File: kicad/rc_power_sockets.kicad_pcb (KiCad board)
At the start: 2 copper layers, 50 x 50 mm, 25 parts, among them IC1 ATTINY85, J1 PIR, J2 433MHZ, J3 433MHZ, P1 ICSP, P2 POWER_IN, Q1 NMOS, Q2 PMOS, U1 MCP1700T

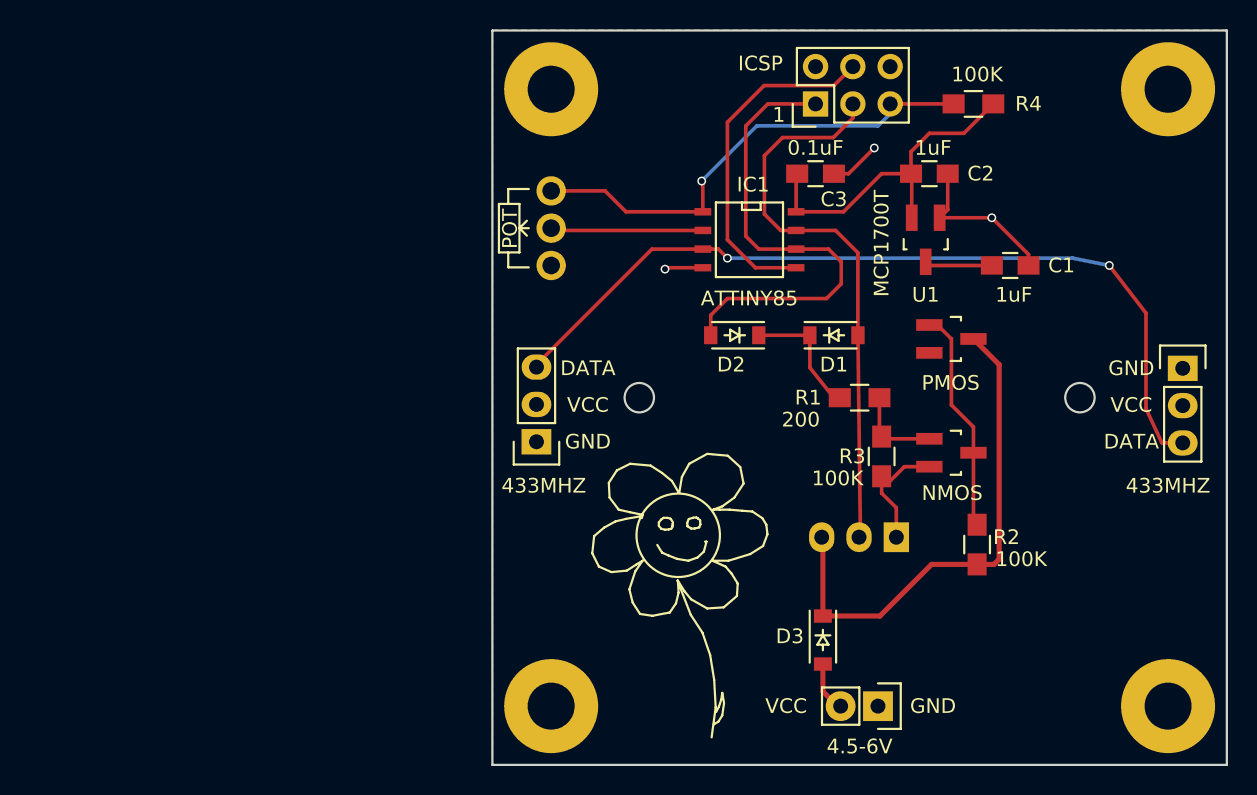
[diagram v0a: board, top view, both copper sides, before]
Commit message: Changed voltage regulator to handle higher input
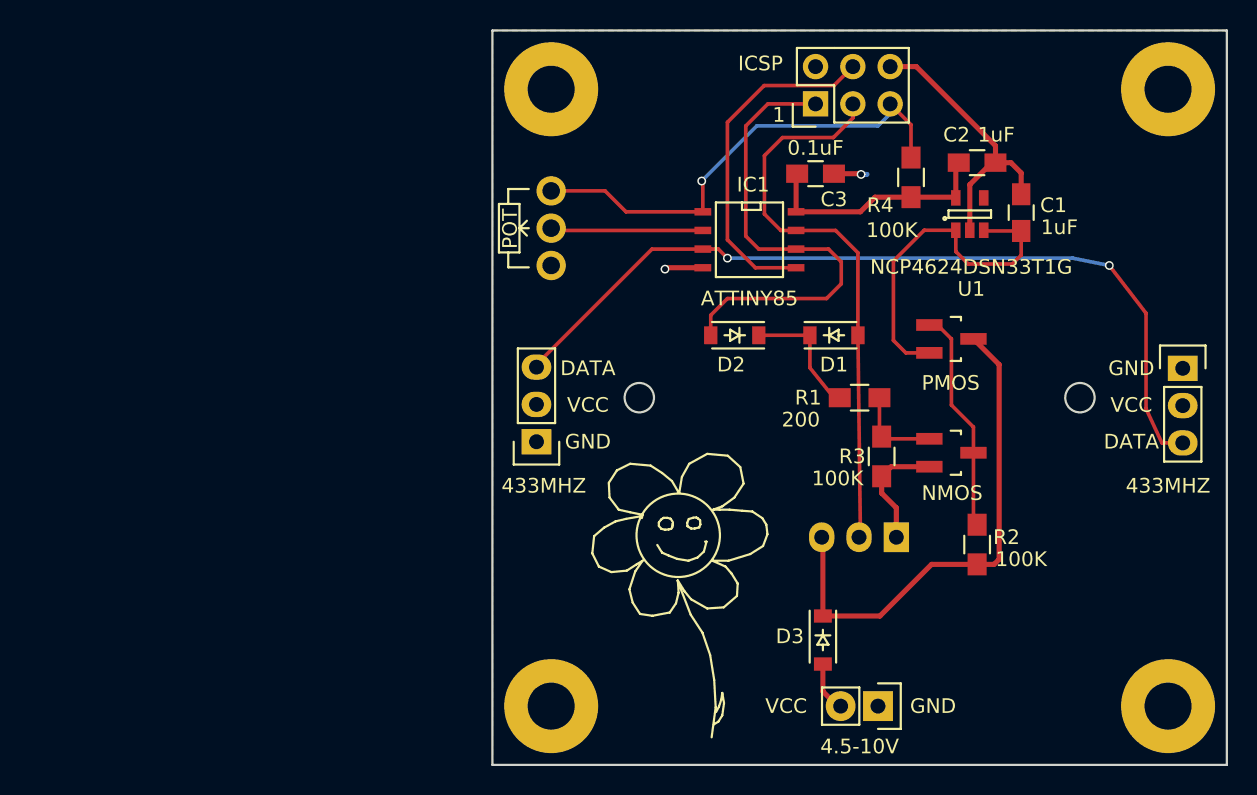
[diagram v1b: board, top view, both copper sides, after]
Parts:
- U1: value MCP1700T -> NCP4624DSN33T1G; footprint TO_SOT_Packages_SMD:SOT-23_Handsoldering -> SOT-23-5
- moved R4 6.56 mm to (148.5, 70.0), turned to 270 degrees
- moved C1 3.68 mm to (156.0, 72.4), turned to 90 degrees
- moved U1 3.47 mm to (152.5, 72.5), turned to 90 degrees
- moved C2 3.34 mm to (153.0, 69.0)
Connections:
- U1 pad 1: GND -> /SWITCH_POWER
- U1 pad 2: /3.3v -> GND
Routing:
- net /SWITCH_POWER: track 4.60 -> 24.0 mm
- net GND: track 25.4 -> 33.1 mm, vias 3 -> 2
- net /3.3v: track 23.0 -> 16.4 mm
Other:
- net class GND added: clearance 0.3, trace_width 0.35, via_dia 0.6, via_drill 0.4
- board text added: "4.5-10V"
- board text removed: "4.5-6V"

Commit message: Silkscreen update
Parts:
- U1: value NCP4624DSN33T1G -> 3.3V REG
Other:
- board text added: "March 2016"
- board text added: "https://github.com/theapi/rc_power_sockets"
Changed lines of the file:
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@@
-(kicad_pcb (version 4) (host pcbnew 4.0.1-stable)
+(kicad_pcb (version 4) (host pcbnew 4.0.2-4+6225~38~ubuntu14.04.1-stable)
   (general
     (links 48)
     (no_connects 0)
-    (area 119.924999 59.924999 170.075001 110.075001)
+    (area 118.275 58.575 171.208334 111.275)
     (thickness 1.6)
-    (drawings 21)
+    (drawings 23)
     (tracks 130)
     (zones 0)
@@
   (layers
     (0 F.Cu signal)
-    (31 B.Cu signal hide)
+    (31 B.Cu signal)
     (32 B.Adhes user)
     (33 F.Adhes user)
@@
     (tags "capacitor 0805")
     (attr smd)
-    (fp_text reference C2 (at -1.4 -1.9 180) (layer F.SilkS)
-      (effects (font (size 1 1) (thickness 0.15)))
-    )
-    (fp_text value 1uF (at 1.3 -1.9) (layer F.SilkS)
+    (fp_text reference C2 (at 1.75 -1.75 180) (layer F.SilkS)
+      (effects (font (size 1 1) (thickness 0.15)))
+    )
+    (fp_text value 1uF (at -1.25 -1.75) (layer F.SilkS)
       (effects (font (size 1 1) (thickness 0.15)))
     )
@@
     (tags "capacitor 0805")
     (attr smd)
-    (fp_text reference C3 (at 1.25 1.75) (layer F.SilkS)
-      (effects (font (size 1 1) (thickness 0.15)))
-    )
-    (fp_text value 0.1uF (at 0 -1.75) (layer F.SilkS)
+    (fp_text reference C3 (at 2.5 -1.75) (layer F.SilkS)
+      (effects (font (size 1 1) (thickness 0.15)))
+    )
+    (fp_text value 0.1uF (at -1 -1.75) (layer F.SilkS)
       (effects (font (size 1 1) (thickness 0.15)))
     )
@@
     (tags SOT-23-5)
     (attr smd)
-    (fp_text reference U1 (at -5.1 0.1 180) (layer F.SilkS)
-      (effects (font (size 1 1) (thickness 0.15)))
-    )
-    (fp_text value NCP4624DSN33T1G (at -3.6 0.1 180) (layer F.SilkS)
+    (fp_text reference U1 (at -3 0 180) (layer F.SilkS)
+      (effects (font (size 1 1) (thickness 0.15)))
+    )
+    (fp_text value "3.3V REG" (at -4.5 0 180) (layer F.SilkS)
       (effects (font (size 1 1) (thickness 0.15)))
     )
@@
     )
   )
+  (gr_text www.theapi.co.uk (at 144.75 85) (layer B.SilkS)
+    (effects (font (size 1 1) (thickness 0.15)) (justify mirror))
+  )
+  (gr_text https://github.com/theapi/rc_power_sockets (at 145.5 78.5) (layer B.SilkS)
+    (effects (font (size 1 1) (thickness 0.15)) (justify mirror))
+  )
   (gr_text 1 (at 139.5 65.75) (layer F.SilkS)
     (effects (font (size 1 1) (thickness 0.15)))
@@
     (effects (font (size 1 1) (thickness 0.15)))
   )
-  (gr_text www.theapi.co.uk (at 144.8 82.6) (layer B.SilkS)
-    (effects (font (size 1 1) (thickness 0.15)) (justify mirror))
-  )
-  (gr_text "RC Power Sockets v1.0" (at 145 80.6) (layer B.SilkS)
+  (gr_text "March 2016" (at 135.75 81) (layer B.SilkS)
     (effects (font (size 1 1) (thickness 0.15) italic) (justify mirror))
   )
+  (gr_text "RC Power Sockets v1.0" (at 150 81) (layer B.SilkS)
+    (effects (font (size 1 1) (thickness 0.15) italic) (justify mirror))
+  )

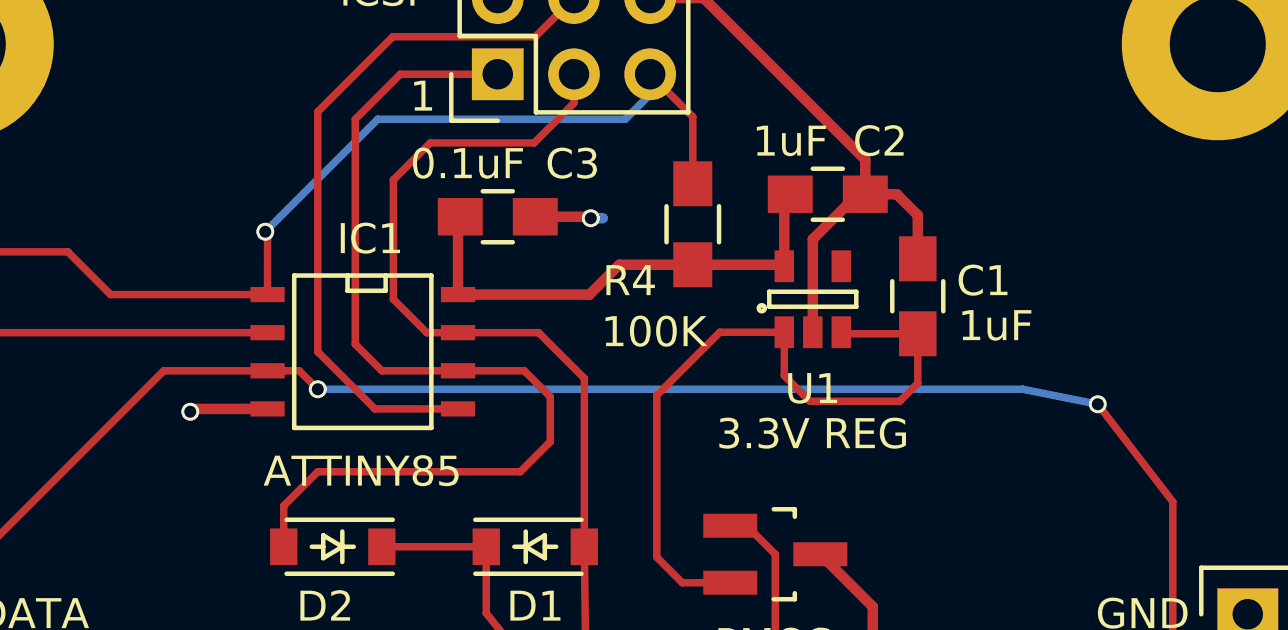
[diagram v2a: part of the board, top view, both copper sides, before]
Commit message: oshpark pcb rules
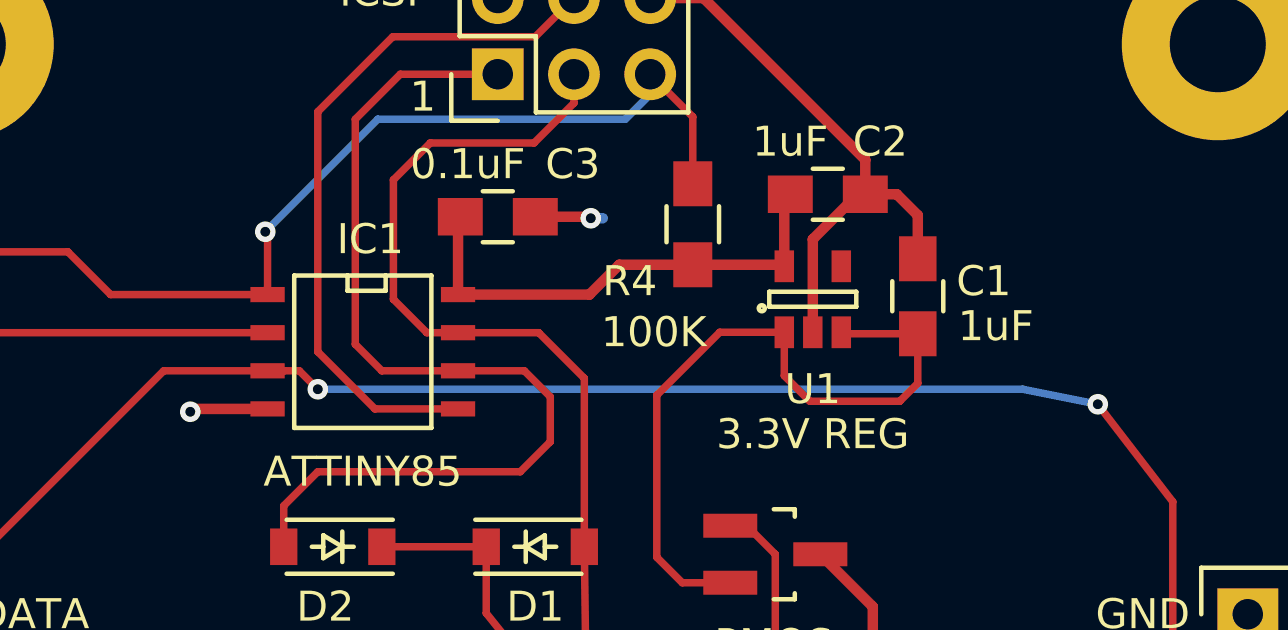
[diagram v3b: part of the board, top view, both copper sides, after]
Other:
- net class Default: via_dia 0.6 -> 0.6858; via_drill 0.4 -> 0.3302
- net class GND: via_dia 0.6 -> 0.6858; via_drill 0.4 -> 0.3302
- net class VCC: via_dia 0.6 -> 0.6858; via_drill 0.4 -> 0.3302
- rule via_min_drill: 0.3 -> 0.3302
- rule via_min_size: 0.4 -> 0.6858
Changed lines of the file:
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@@
     (segment_width 0.2)
     (edge_width 0.15)
-    (via_size 0.6)
-    (via_drill 0.4)
-    (via_min_size 0.4)
-    (via_min_drill 0.3)
-    (uvia_size 0.3)
-    (uvia_drill 0.1)
+    (via_size 0.6858)
+    (via_drill 0.3302)
+    (via_min_size 0.6858)
+    (via_min_drill 0.3302)
+    (uvia_size 0.508)
+    (uvia_drill 0.127)
     (uvias_allowed no)
-    (uvia_min_size 0.2)
-    (uvia_min_drill 0.1)
+    (uvia_min_size 0.508)
+    (uvia_min_drill 0.127)
     (pcb_text_width 0.3)
     (pcb_text_size 1.5 1.5)
@@
     (clearance 0.2)
     (trace_width 0.25)
-    (via_dia 0.6)
-    (via_drill 0.4)
-    (uvia_dia 0.3)
-    (uvia_drill 0.1)
+    (via_dia 0.6858)
+    (via_drill 0.3302)
+    (uvia_dia 0.508)
+    (uvia_drill 0.127)
     (add_net /ADC3)
     (add_net /MISO)
@@
     (clearance 0.3)
     (trace_width 0.35)
-    (via_dia 0.6)
-    (via_drill 0.4)
-    (uvia_dia 0.3)
-    (uvia_drill 0.1)
+    (via_dia 0.6858)
+    (via_drill 0.3302)
+    (uvia_dia 0.508)
+    (uvia_drill 0.127)
     (add_net GND)
   )
@@
     (clearance 0.3)
     (trace_width 0.35)
-    (via_dia 0.6)
-    (via_drill 0.4)
-    (uvia_dia 0.3)
-    (uvia_drill 0.1)
+    (via_dia 0.6858)
+    (via_drill 0.3302)
+    (uvia_dia 0.508)
+    (uvia_drill 0.127)
     (add_net /3.3v)
     (add_net /POWER)
@@
   (segment (start 143.25 69.75) (end 145.05 69.75) (width 0.35) (layer F.Cu) (net 1))
   (segment (start 145.05 69.75) (end 145.1 69.8) (width 0.35) (layer F.Cu) (net 1))
-  (via (at 145.1 69.8) (size 0.6) (drill 0.4) (layers F.Cu B.Cu) (net 1))
+  (via (at 145.1 69.8) (size 0.6858) (drill 0.3302) (layers F.Cu B.Cu) (net 1))
   (segment (start 145.1 69.8) (end 145.5 69.8) (width 0.35) (layer B.Cu) (net 1))
   (segment (start 147.08 62.46) (end 147.08 62.52) (width 0.25) (layer F.Cu) (net 1))
@@
   (segment (start 134.325 76.155) (end 131.845 76.155) (width 0.35) (layer F.Cu) (net 1))
   (segment (start 131.845 76.155) (end 131.75 76.25) (width 0.35) (layer F.Cu) (net 1))
-  (via (at 131.75 76.25) (size 0.6) (drill 0.4) (layers F.Cu B.Cu) (net 1))
+  (via (at 131.75 76.25) (size 0.6858) (drill 0.3302) (layers F.Cu B.Cu) (net 1))
   (segment (start 144.885 80.75) (end 145.065 95.145) (width 0.25) (layer F.Cu) (net 2) (status 20))
   (segment (start 145.065 95.145) (end 144.96 95.25) (width 0.25) (layer F.Cu) (net 2) (status 30))
@@
   (segment (start 134.325 70.325) (end 134.325 72.345) (width 0.25) (layer F.Cu) (net 4))
   (segment (start 134.25 70.25) (end 134.325 70.325) (width 0.25) (layer F.Cu) (net 4))
-  (via (at 134.25 70.25) (size 0.6) (drill 0.4) (layers F.Cu B.Cu) (net 4))
+  (via (at 134.25 70.25) (size 0.6858) (drill 0.3302) (layers F.Cu B.Cu) (net 4))
   (segment (start 138 66.5) (end 134.25 70.25) (width 0.25) (layer B.Cu) (net 4))
   (segment (start 146.25 66.5) (end 138 66.5) (width 0.25) (layer B.Cu) (net 4))
@@
   (segment (start 135.385 74.885) (end 134.325 74.885) (width 0.25) (layer F.Cu) (net 5))
   (segment (start 136 75.5) (end 135.385 74.885) (width 0.25) (layer F.Cu) (net 5))
-  (via (at 136 75.5) (size 0.6) (drill 0.4) (layers F.Cu B.Cu) (net 5))
+  (via (at 136 75.5) (size 0.6858) (drill 0.3302) (layers F.Cu B.Cu) (net 5))
   (segment (start 159.5 75.5) (end 136 75.5) (width 0.25) (layer B.Cu) (net 5))
   (segment (start 162 76) (end 159.5 75.5) (width 0.25) (layer B.Cu) (net 5))
-  (via (at 162 76) (size 0.6) (drill 0.4) (layers F.Cu B.Cu) (net 5))
+  (via (at 162 76) (size 0.6858) (drill 0.3302) (layers F.Cu B.Cu) (net 5))
   (segment (start 164.5 79.25) (end 162 76) (width 0.25) (layer F.Cu) (net 5))
   (segment (start 164.5 85.75) (end 164.5 79.25) (width 0.25) (layer F.Cu) (net 5))

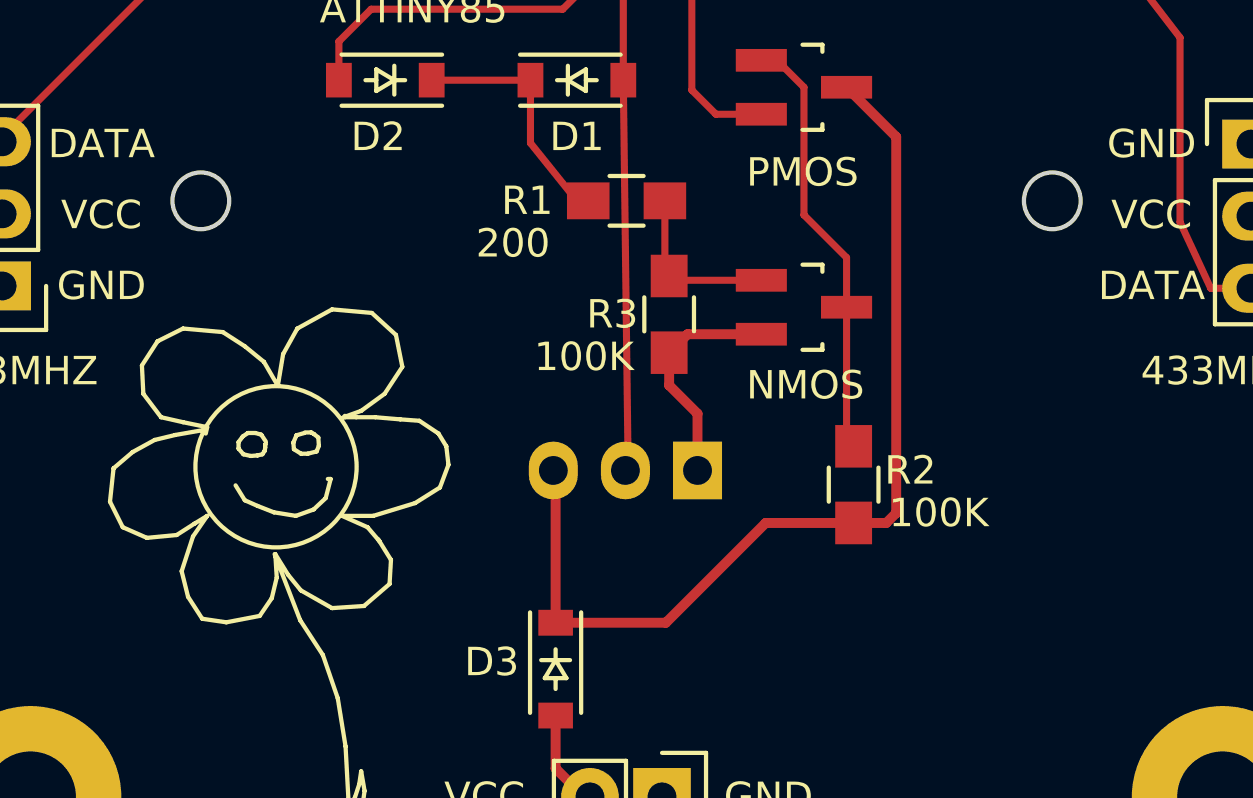
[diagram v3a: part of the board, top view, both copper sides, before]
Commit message: Positioned the PIR mounting
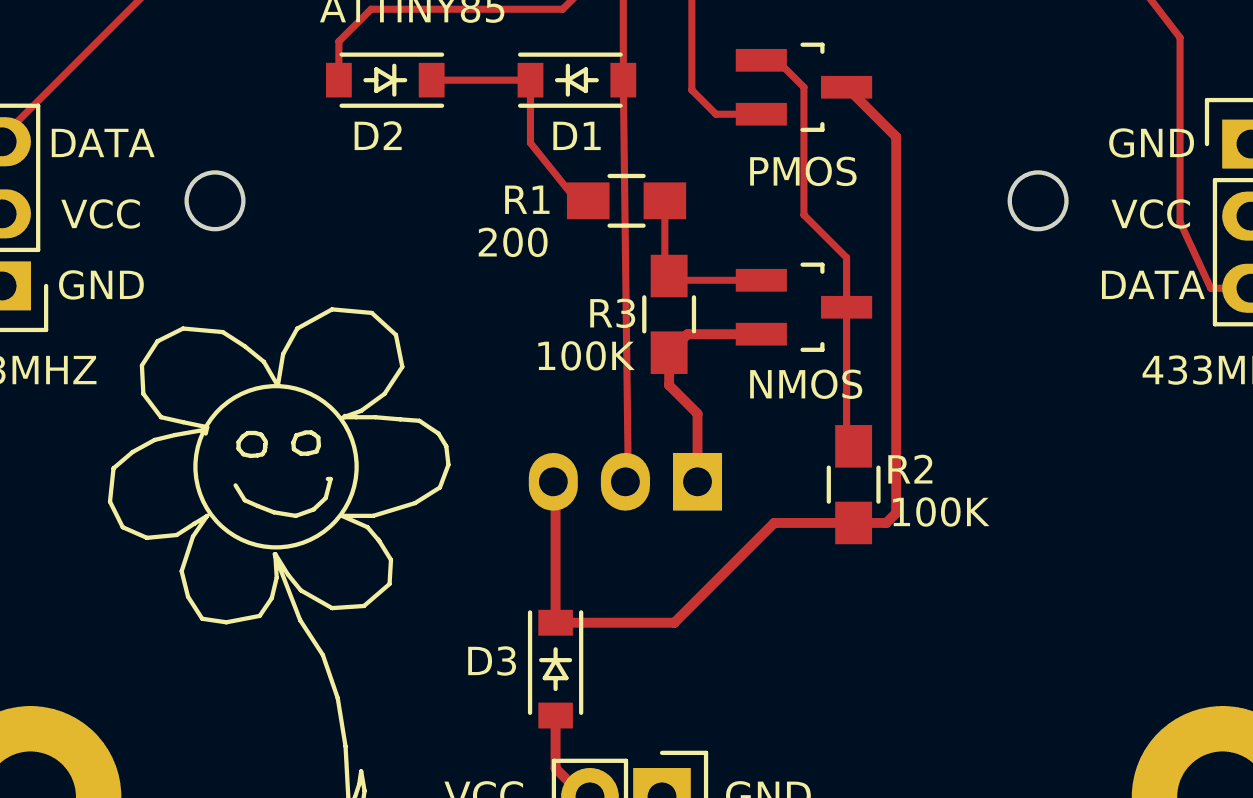
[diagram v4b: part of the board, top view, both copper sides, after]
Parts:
- moved J1 0.40 mm to (147.5, 94.9)
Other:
- outline, holes or cut-outs redrawn
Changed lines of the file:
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@@
     (area 118.275 58.575 171.208334 111.275)
     (thickness 1.6)
-    (drawings 23)
-    (tracks 130)
+    (drawings 24)
+    (tracks 131)
     (zones 0)
     (modules 25)
@@
   )
   (module Socket_Strips:Socket_Strip_Straight_1x03 (layer B.Cu)
-    (at 147.5 94.5 180)
+    (at 147.5 94.9 180)
     (descr "Through hole socket strip")
     (tags "socket strip")
@@
     )
   )
+  (dimension 10.004499 (width 0.3) (layer F.Mask)
+    (gr_text "10.004 mm" (at 156.717032 90.087989 271.718358) (layer F.Mask)
+      (effects (font (size 1.5 1.5) (thickness 0.3)))
+    )
+    (feature1 (pts (xy 159.8 95) (xy 155.517639 95.128471)))
+    (feature2 (pts (xy 159.5 85) (xy 155.217639 85.128471)))
+    (crossbar (pts (xy 157.916425 85.047507) (xy 158.216425 95.047507)))
+    (arrow1a (pts (xy 158.216425 95.047507) (xy 157.596488 93.939095)))
+    (arrow1b (pts (xy 158.216425 95.047507) (xy 158.768802 93.903925)))
+    (arrow2a (pts (xy 157.916425 85.047507) (xy 157.364048 86.191089)))
+    (arrow2b (pts (xy 157.916425 85.047507) (xy 158.536362 86.155919)))
+  )
   (gr_text www.theapi.co.uk (at 144.75 85) (layer B.SilkS)
     (effects (font (size 1 1) (thickness 0.15)) (justify mirror))
@@
     (effects (font (size 1 1) (thickness 0.15)) (justify mirror))
   )
-  (gr_circle (center 130 85) (end 130 84) (layer Edge.Cuts) (width 0.15))
-  (gr_circle (center 160 85) (end 160 84) (layer Edge.Cuts) (width 0.15))
+  (gr_circle (center 130.5 85) (end 130.5 84) (layer Edge.Cuts) (width 0.15))
+  (gr_circle (center 159.5 85) (end 159.5 84) (layer Edge.Cuts) (width 0.15))
   (gr_line (start 120 110) (end 120 60) (angle 90) (layer Edge.Cuts) (width 0.15))
   (gr_line (start 170 110) (end 120 110) (angle 90) (layer Edge.Cuts) (width 0.15))
@@
   (segment (start 141.615 82.965) (end 143.65 85.5) (width 0.25) (layer F.Cu) (net 13) (status 20))
   (segment (start 138.135 80.75) (end 141.615 80.75) (width 0.25) (layer F.Cu) (net 13))
-  (segment (start 153 96.35) (end 149.9 96.35) (width 0.35) (layer F.Cu) (net 14))
-  (segment (start 146.385 99.865) (end 142.5 99.865) (width 0.35) (layer F.Cu) (net 14))
-  (segment (start 149.9 96.35) (end 146.385 99.865) (width 0.35) (layer F.Cu) (net 14))
-  (segment (start 142.5 99.865) (end 142.5 94.58) (width 0.35) (layer F.Cu) (net 14))
+  (segment (start 153 96.35) (end 150.2 96.35) (width 0.35) (layer F.Cu) (net 14) (status 400000))
+  (segment (start 146.685 99.865) (end 142.5 99.865) (width 0.35) (layer F.Cu) (net 14) (status 800000))
+  (segment (start 150.2 96.35) (end 146.685 99.865) (width 0.35) (layer F.Cu) (net 14))
+  (segment (start 142.5 99.865) (end 142.5 94.98) (width 0.35) (layer F.Cu) (net 14) (status C00000))
+  (segment (start 142.5 94.98) (end 142.42 94.9) (width 0.35) (layer F.Cu) (net 14) (status C00000))
   (segment (start 142.5 94.58) (end 142.42 94.5) (width 0.25) (layer F.Cu) (net 14))
   (segment (start 153 96.35) (end 154.15 96.35) (width 0.35) (layer F.Cu) (net 14))

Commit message: Silkscreen changes
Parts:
- added REF**: TheApiLogo, theapi_footprints:TheApiLogo, B.Cu at (145.0, 69.0)
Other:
- board text added: "RC Power Sockets v1.0 - March 2016"
- board text removed: "March 2016"
- board text removed: "RC Power Sockets v1.0"
- board text removed: "www.theapi.co.uk"
